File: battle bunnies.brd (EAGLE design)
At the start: 151.7 x 94 mm, 59 parts, among them IC1 CP2104, Q1 mmbt2222, Q2 mmbt2222, SW2 KMR2, U1 PCA9685, U2 SPX3819, U3 MCP73831T-2ACI/OT, X2 ESP-12, X4 20329

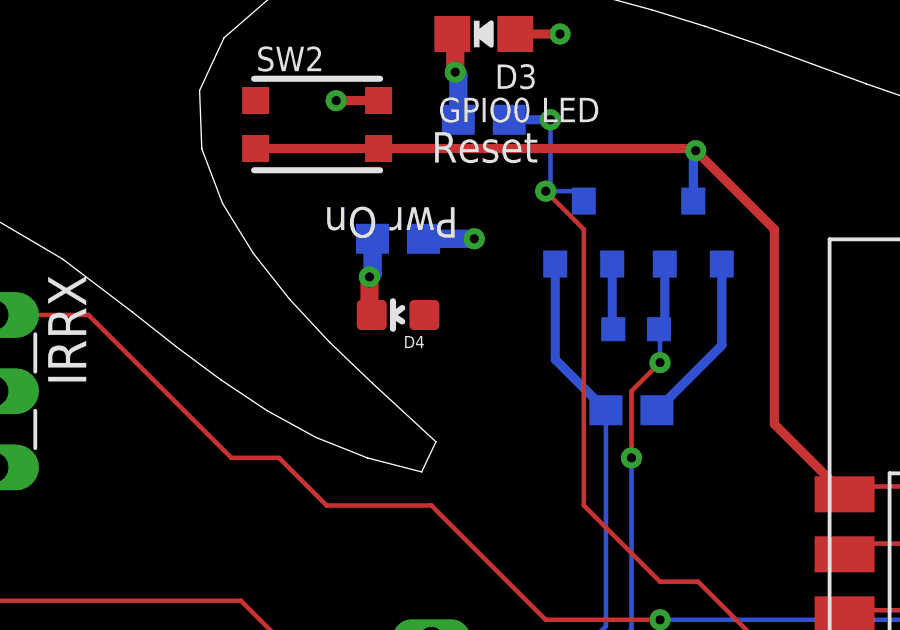
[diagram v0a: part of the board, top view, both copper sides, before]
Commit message: Fixing Power LED
Right now the 'Power LED' is run from Ground to... Ground, so it's
not exactly going to work 'right'.  When moving things around in
Eagle it didn't attach properly to the 3.3V line on the schematic
and so was left dangling, despite it being connected.

This, thankfully, doesn't affect the boards except cause a little
bit of build waste.  This is fixed now, though it'll likely get
set to DNI, as it's only really useful on dev boards.
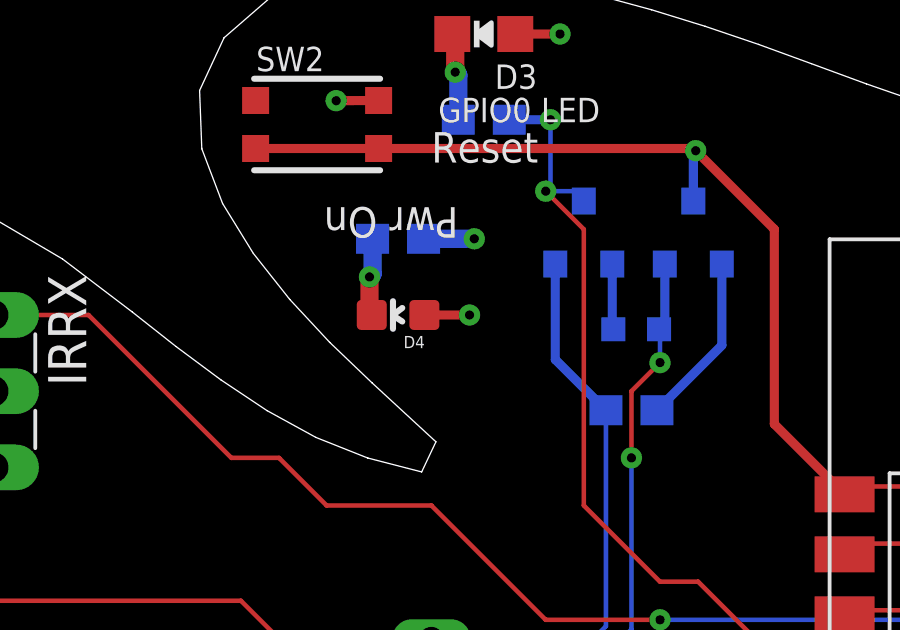
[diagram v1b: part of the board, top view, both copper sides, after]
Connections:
- removed net N$11: D4.A
- net 3.3V: now also D4.A
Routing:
- net 3.3V: track 3.04 -> 4.54 mm, vias 2 -> 3
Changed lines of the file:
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@@
 <wire x1="34.0925" y1="54.9525" x2="32.54375" y2="54.9275" width="0.6096" layer="1"/>
 <via x="32.54375" y="54.9275" extent="1-16" drill="0.3048"/>
+<contactref element="D4" pad="A"/>
+<wire x1="20.08575" y1="74.93" x2="21.59" y2="74.93" width="0.3048" layer="1"/>
+<via x="21.59" y="74.93" extent="1-16" drill="0.3048"/>
 </signal>
 <signal name="RESET">
@@
 <wire x1="30.546" y1="23.1115" x2="32.258" y2="21.3995" width="0.4064" layer="16"/>
 </signal>
-<signal name="N$11">
-<contactref element="D4" pad="A"/>
-</signal>
 <signal name="PWM0">

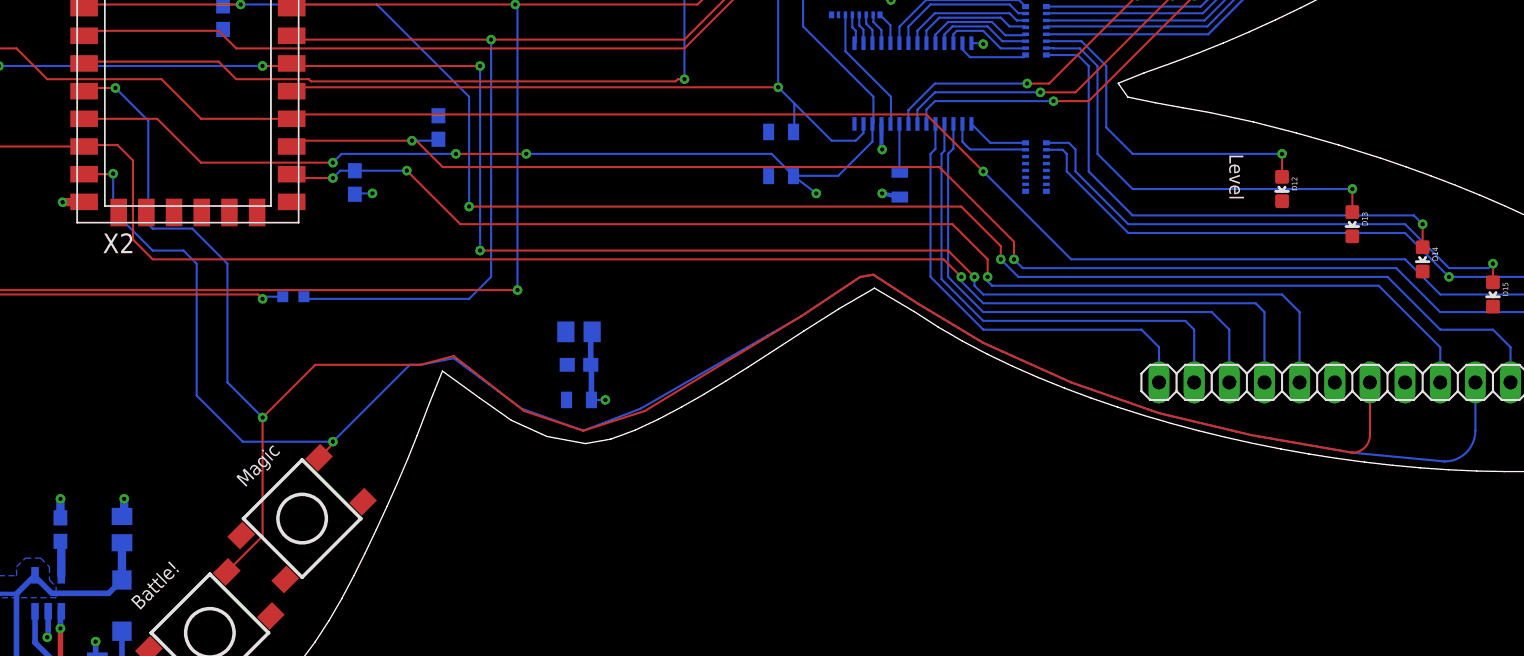
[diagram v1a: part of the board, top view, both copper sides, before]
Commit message: Flipping GPIO16 with GPIO15 on the 'Battle' Button
GPIO16 *APPARENTLY* doesn't actually have hard interrupt
support, which makes it slightly obnoxious for the 'battle'
button, which should be there to wake the bunny from a sleep
state, or get it to do something.
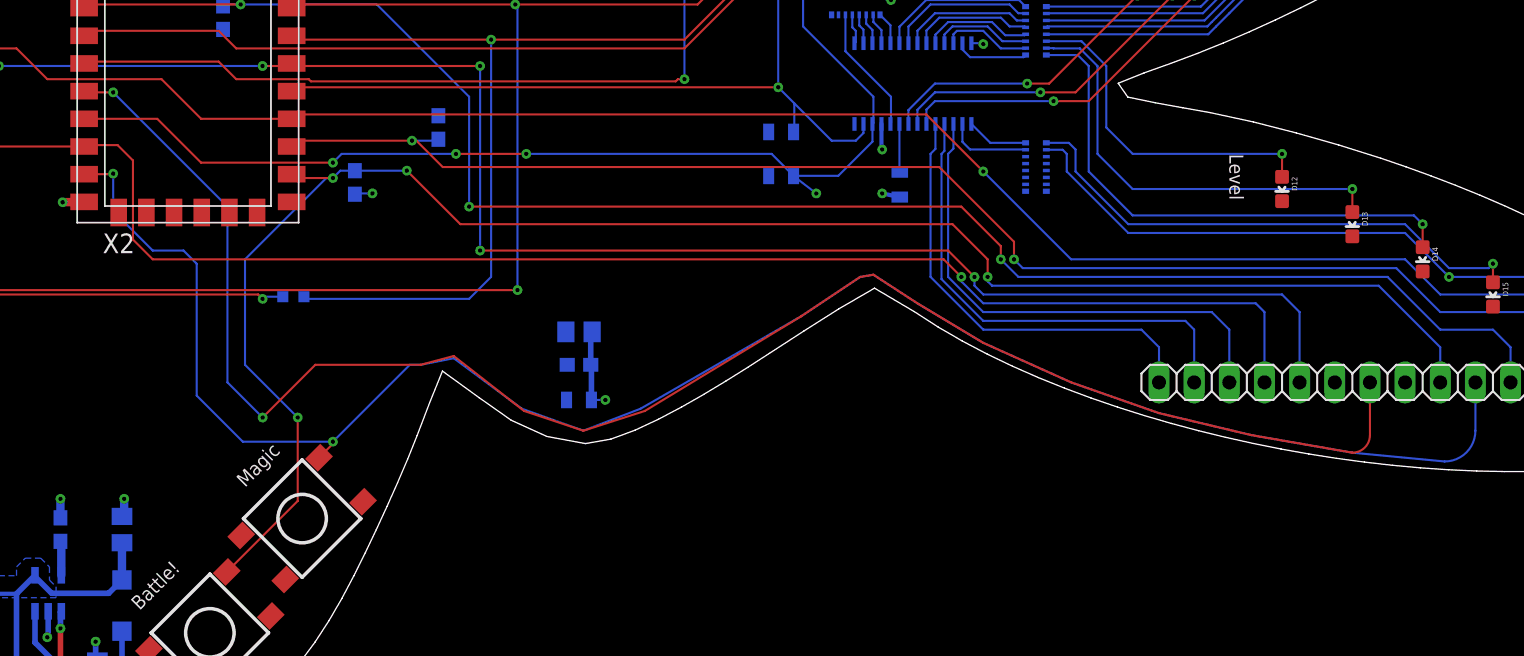
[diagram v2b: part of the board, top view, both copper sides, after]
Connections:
- net GPIO15: now also S3.B2
- net GPIO16: no longer S3.B2
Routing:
- net GPIO15: track 93.5 -> 127.3 mm, vias 3 -> 4
- net GPIO16: track 137.8 -> 123.7 mm
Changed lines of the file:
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@@
 <layer number="155" name="FabDoc3" color="7" fill="1" visible="yes" active="yes"/>
 <layer number="199" name="Contour" color="7" fill="1" visible="yes" active="yes"/>
-<layer number="200" name="200bmp" color="1" fill="10" visible="yes" active="yes"/>
-<layer number="201" name="201bmp" color="2" fill="10" visible="yes" active="yes"/>
-<layer number="202" name="202bmp" color="3" fill="10" visible="yes" active="yes"/>
-<layer number="203" name="203bmp" color="4" fill="10" visible="yes" active="yes"/>
-<layer number="204" name="204bmp" color="5" fill="10" visible="yes" active="yes"/>
-<layer number="205" name="205bmp" color="6" fill="10" visible="yes" active="yes"/>
-<layer number="206" name="206bmp" color="7" fill="10" visible="yes" active="yes"/>
-<layer number="207" name="207bmp" color="8" fill="10" visible="yes" active="yes"/>
-<layer number="208" name="208bmp" color="9" fill="10" visible="yes" active="yes"/>
-<layer number="209" name="209bmp" color="10" fill="10" visible="yes" active="yes"/>
-<layer number="210" name="210bmp" color="11" fill="10" visible="yes" active="yes"/>
-<layer number="211" name="211bmp" color="12" fill="10" visible="yes" active="yes"/>
-<layer number="212" name="212bmp" color="13" fill="10" visible="yes" active="yes"/>
-<layer number="213" name="213bmp" color="14" fill="10" visible="yes" active="yes"/>
-<layer number="214" name="214bmp" color="15" fill="10" visible="yes" active="yes"/>
-<layer number="215" name="215bmp" color="16" fill="10" visible="yes" active="yes"/>
-<layer number="216" name="216bmp" color="7" fill="1" visible="yes" active="yes"/>
+<layer number="200" name="200bmp" color="1" fill="10" visible="no" active="yes"/>
+<layer number="201" name="201bmp" color="2" fill="10" visible="no" active="yes"/>
+<layer number="202" name="202bmp" color="3" fill="10" visible="no" active="yes"/>
+<layer number="203" name="203bmp" color="4" fill="10" visible="no" active="yes"/>
+<layer number="204" name="204bmp" color="5" fill="10" visible="no" active="yes"/>
+<layer number="205" name="205bmp" color="6" fill="10" visible="no" active="yes"/>
+<layer number="206" name="206bmp" color="7" fill="10" visible="no" active="yes"/>
+<layer number="207" name="207bmp" color="8" fill="10" visible="no" active="yes"/>
+<layer number="208" name="208bmp" color="9" fill="10" visible="no" active="yes"/>
+<layer number="209" name="209bmp" color="10" fill="10" visible="no" active="yes"/>
+<layer number="210" name="210bmp" color="11" fill="10" visible="no" active="yes"/>
+<layer number="211" name="211bmp" color="12" fill="10" visible="no" active="yes"/>
+<layer number="212" name="212bmp" color="13" fill="10" visible="no" active="yes"/>
+<layer number="213" name="213bmp" color="14" fill="10" visible="no" active="yes"/>
+<layer number="214" name="214bmp" color="15" fill="10" visible="no" active="yes"/>
+<layer number="215" name="215bmp" color="16" fill="10" visible="no" active="yes"/>
+<layer number="216" name="216bmp" color="7" fill="1" visible="no" active="yes"/>
 <layer number="217" name="217bmp" color="18" fill="1" visible="no" active="no"/>
 <layer number="218" name="218bmp" color="19" fill="1" visible="no" active="no"/>
@@
 <layer number="223" name="223bmp" color="24" fill="1" visible="no" active="no"/>
 <layer number="224" name="224bmp" color="25" fill="1" visible="no" active="no"/>
-<layer number="225" name="225bmp" color="7" fill="1" visible="yes" active="yes"/>
-<layer number="226" name="226bmp" color="7" fill="1" visible="yes" active="yes"/>
-<layer number="227" name="227bmp" color="7" fill="1" visible="yes" active="yes"/>
-<layer number="228" name="228bmp" color="7" fill="1" visible="yes" active="yes"/>
-<layer number="229" name="229bmp" color="7" fill="1" visible="yes" active="yes"/>
-<layer number="230" name="230bmp" color="7" fill="1" visible="yes" active="yes"/>
-<layer number="231" name="231bmp" color="7" fill="1" visible="yes" active="yes"/>
+<layer number="225" name="225bmp" color="7" fill="1" visible="no" active="yes"/>
+<layer number="226" name="226bmp" color="7" fill="1" visible="no" active="yes"/>
+<layer number="227" name="227bmp" color="7" fill="1" visible="no" active="yes"/>
+<layer number="228" name="228bmp" color="7" fill="1" visible="no" active="yes"/>
+<layer number="229" name="229bmp" color="7" fill="1" visible="no" active="yes"/>
+<layer number="230" name="230bmp" color="7" fill="1" visible="no" active="yes"/>
+<layer number="231" name="231bmp" color="7" fill="1" visible="no" active="yes"/>
 <layer number="232" name="Eagle3D_PG2" color="7" fill="1" visible="no" active="no"/>
 <layer number="233" name="Eagle3D_PG3" color="7" fill="1" visible="no" active="no"/>
-<layer number="248" name="Housing" color="7" fill="1" visible="yes" active="yes"/>
-<layer number="249" name="Edge" color="7" fill="1" visible="yes" active="yes"/>
+<layer number="248" name="Housing" color="7" fill="1" visible="no" active="yes"/>
+<layer number="249" name="Edge" color="7" fill="1" visible="no" active="yes"/>
 <layer number="250" name="Descript" color="3" fill="1" visible="no" active="no"/>
 <layer number="251" name="SMDround" color="12" fill="11" visible="no" active="no"/>
-<layer number="254" name="cooling" color="7" fill="1" visible="yes" active="yes"/>
-<layer number="255" name="routoute" color="7" fill="1" visible="yes" active="yes"/>
+<layer number="254" name="cooling" color="7" fill="1" visible="no" active="yes"/>
+<layer number="255" name="routoute" color="7" fill="1" visible="no" active="yes"/>
 </layers>
 <board>
@@
 <signal name="GPIO16">
 <contactref element="X2" pad="4"/>
-<contactref element="S3" pad="B2"/>
 <contactref element="JP2" pad="9"/>
-<wire x1="127" y1="41.91" x2="127" y2="38.1" width="0.1524" layer="1"/>
 <wire x1="127" y1="38.1" x2="125.73" y2="36.83" width="0.1524" layer="1" curve="-90"/>
 <wire x1="125.73" y1="36.83" x2="118.4275" y2="38.1" width="0.1524" layer="1"/>
@@
 <wire x1="65.88125" y1="39.84625" x2="60.80125" y2="43.815" width="0.1524" layer="1"/>
 <wire x1="60.80125" y1="43.815" x2="58.42" y2="43.18" width="0.1524" layer="1"/>
-<wire x1="44.45" y1="50.4825" x2="44.45" y2="41.91" width="0.1524" layer="16"/>
+<wire x1="44.45" y1="54.61" x2="44.45" y2="41.91" width="0.1524" layer="16"/>
 <wire x1="44.45" y1="41.91" x2="46.99" y2="39.37" width="0.1524" layer="16"/>
-<wire x1="44.45" y1="50.4825" x2="41.91" y2="53.0225" width="0.1524" layer="16"/>
-<wire x1="41.91" y1="53.0225" x2="39.0525" y2="53.0225" width="0.1524" layer="16"/>
-<wire x1="39.0525" y1="53.0225" x2="38.735" y2="53.34" width="0.1524" layer="16"/>
 <wire x1="34.3225" y1="63.1825" x2="34.0925" y2="62.9525" width="0.1524" layer="1" curve="90"/>
-<wire x1="34.3225" y1="63.1825" x2="36.35375" y2="63.1825" width="0.1524" layer="1"/>
-<via x="36.35375" y="63.1825" extent="1-16" drill="0.3048" diameter="0.3048"/>
-<wire x1="38.735" y1="60.80125" x2="38.735" y2="53.34" width="0.1524" layer="16"/>
 <wire x1="58.42" y1="43.18" x2="50.8" y2="43.18" width="0.1524" layer="1"/>
 <wire x1="50.8" y1="43.18" x2="46.99" y2="39.37" width="0.1524" layer="1"/>
 <via x="46.99" y="39.37" extent="1-16" drill="0.3048" diameter="0.3048"/>
-<wire x1="46.99" y1="39.37" x2="46.99" y2="30.80448125" width="0.1524" layer="1"/>
-<wire x1="46.99" y1="30.80448125" x2="44.39975625" y2="28.2142375" width="0.1524" layer="1"/>
-<wire x1="36.35375" y1="63.1825" x2="38.735" y2="60.80125" width="0.1524" layer="16"/>
+<wire x1="127" y1="38.1" x2="127" y2="41.91" width="0.1524" layer="1"/>
+<wire x1="44.45" y1="54.61" x2="36.195" y2="62.865" width="0.1524" layer="16"/>
+<via x="36.195" y="62.865" extent="1-16" drill="0.3048"/>
+<wire x1="36.195" y1="62.865" x2="34.18" y2="62.865" width="0.1524" layer="1"/>
+<wire x1="34.18" y1="62.865" x2="34.0925" y2="62.9525" width="0.1524" layer="1"/>
 </signal>
 <signal name="GPIO15">
@@
 <wire x1="99.3775" y1="49.53" x2="99.3775" y2="49.2125" width="0.1524" layer="16"/>
 <wire x1="99.3775" y1="49.2125" x2="99.695" y2="48.895" width="0.1524" layer="16"/>
-<wire x1="132.08" y1="43.18" x2="132.08" y2="41.91" width="0.1524" layer="16"/>
 <wire x1="61.2775" y1="53.34" x2="96.8375" y2="53.34" width="0.1524" layer="1"/>
 <wire x1="96.8375" y1="53.34" x2="99.3775" y2="50.8" width="0.1524" layer="1"/>
 <wire x1="99.695" y1="48.895" x2="127.635" y2="48.895" width="0.1524" layer="16"/>
 <wire x1="127.635" y1="48.895" x2="132.08" y2="44.45" width="0.1524" layer="16"/>
-<wire x1="132.08" y1="44.45" x2="132.08" y2="41.91" width="0.1524" layer="16"/>
 <wire x1="61.2775" y1="53.34" x2="57.41125" y2="57.20625" width="0.1524" layer="1"/>
 <wire x1="49.29" y1="57.15" x2="49.76625" y2="56.67375" width="0.1524" layer="1"/>
-<wire x1="49.76625" y1="56.67375" x2="52.07" y2="56.67375" width="0.1524" layer="1"/>
 <via x="52.07" y="56.67375" extent="1-16" drill="0.3048" diameter="0.3048"/>
 <wire x1="52.07" y1="56.67375" x2="52.6025" y2="57.20625" width="0.1524" layer="16"/>
@@
 <wire x1="53.6575" y1="57.20625" x2="57.41125" y2="57.20625" width="0.1524" layer="16"/>
 <via x="57.41125" y="57.20625" extent="1-16" drill="0.3048" diameter="0.3048"/>
+<contactref element="S3" pad="B2"/>
+<wire x1="132.08" y1="44.45" x2="132.08" y2="41.91" width="0.1524" layer="16"/>
+<wire x1="49.76625" y1="56.67375" x2="52.07" y2="56.67375" width="0.1524" layer="1"/>
+<wire x1="44.39975625" y1="28.2142375" x2="49.53" y2="33.34448125" width="0.1524" layer="1"/>
+<wire x1="49.53" y1="33.34448125" x2="49.53" y2="39.37" width="0.1524" layer="1"/>
+<via x="49.53" y="39.37" extent="1-16" drill="0.3048"/>
+<wire x1="49.53" y1="39.37" x2="45.72" y2="43.18" width="0.1524" layer="16"/>
+<wire x1="45.72" y1="43.18" x2="45.72" y2="50.8" width="0.1524" layer="16"/>
+<wire x1="45.72" y1="50.8" x2="51.59375" y2="56.67375" width="0.1524" layer="16"/>
+<wire x1="51.59375" y1="56.67375" x2="52.07" y2="56.67375" width="0.1524" layer="16"/>
 </signal>
 <signal name="GPIO0">

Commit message: Marking the "Power On" LEDs as DNI
They aren't needed and adding them is more a debugging
nicety vs. a critical need.
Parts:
- D4: value RED -> RED (DNI)
- R16: value 200 -> 200Ohm (DNI)
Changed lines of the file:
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@@
 </element>
 <element name="D3" library="microbuilder" package="CHIPLED_0805_NOOUTLINE" value="RED" x="22.06625" y="84.29625" rot="R90"/>
-<element name="D4" library="SparkFun-LED" package="LED-0603" value="RED" x="19.20875" y="74.93" rot="R90">
+<element name="D4" library="SparkFun-LED" package="LED-0603" value="RED (DNI)" x="19.20875" y="74.93" rot="R90">
 <attribute name="PROD_ID" value="DIO-00819" x="19.20875" y="74.93" size="1.778" layer="27" rot="R90" display="off"/>
 </element>
@@
 <attribute name="PROD_ID" value="RES-07856" x="5.842" y="21.1455" size="1.778" layer="28" rot="MR90" display="off"/>
 </element>
-<element name="R16" library="SparkFun-Resistors" package="0603-RES" value="200" x="19.20875" y="77.47" rot="MR180">
+<element name="R16" library="SparkFun-Resistors" package="0603-RES" value="200Ohm (DNI)" x="19.20875" y="77.47" rot="MR180">
 <attribute name="PROD_ID" value="RES-08220" x="19.20875" y="77.47" size="1.778" layer="28" rot="MR180" display="off"/>
 </element>
